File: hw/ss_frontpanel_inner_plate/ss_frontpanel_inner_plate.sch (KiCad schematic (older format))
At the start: 32 parts, among them J1 FFC_conn_14p, J2 FFC_conn_14p, J3 FFC_conn_14p, M1 Mousebite_stamp_holes, M2 Mousebite_stamp_holes, M3 Mousebite_stamp_holes, M4 FFC_retention_clamp, M5 FFC_retention_clamp, U6 TLV9051SIDBV

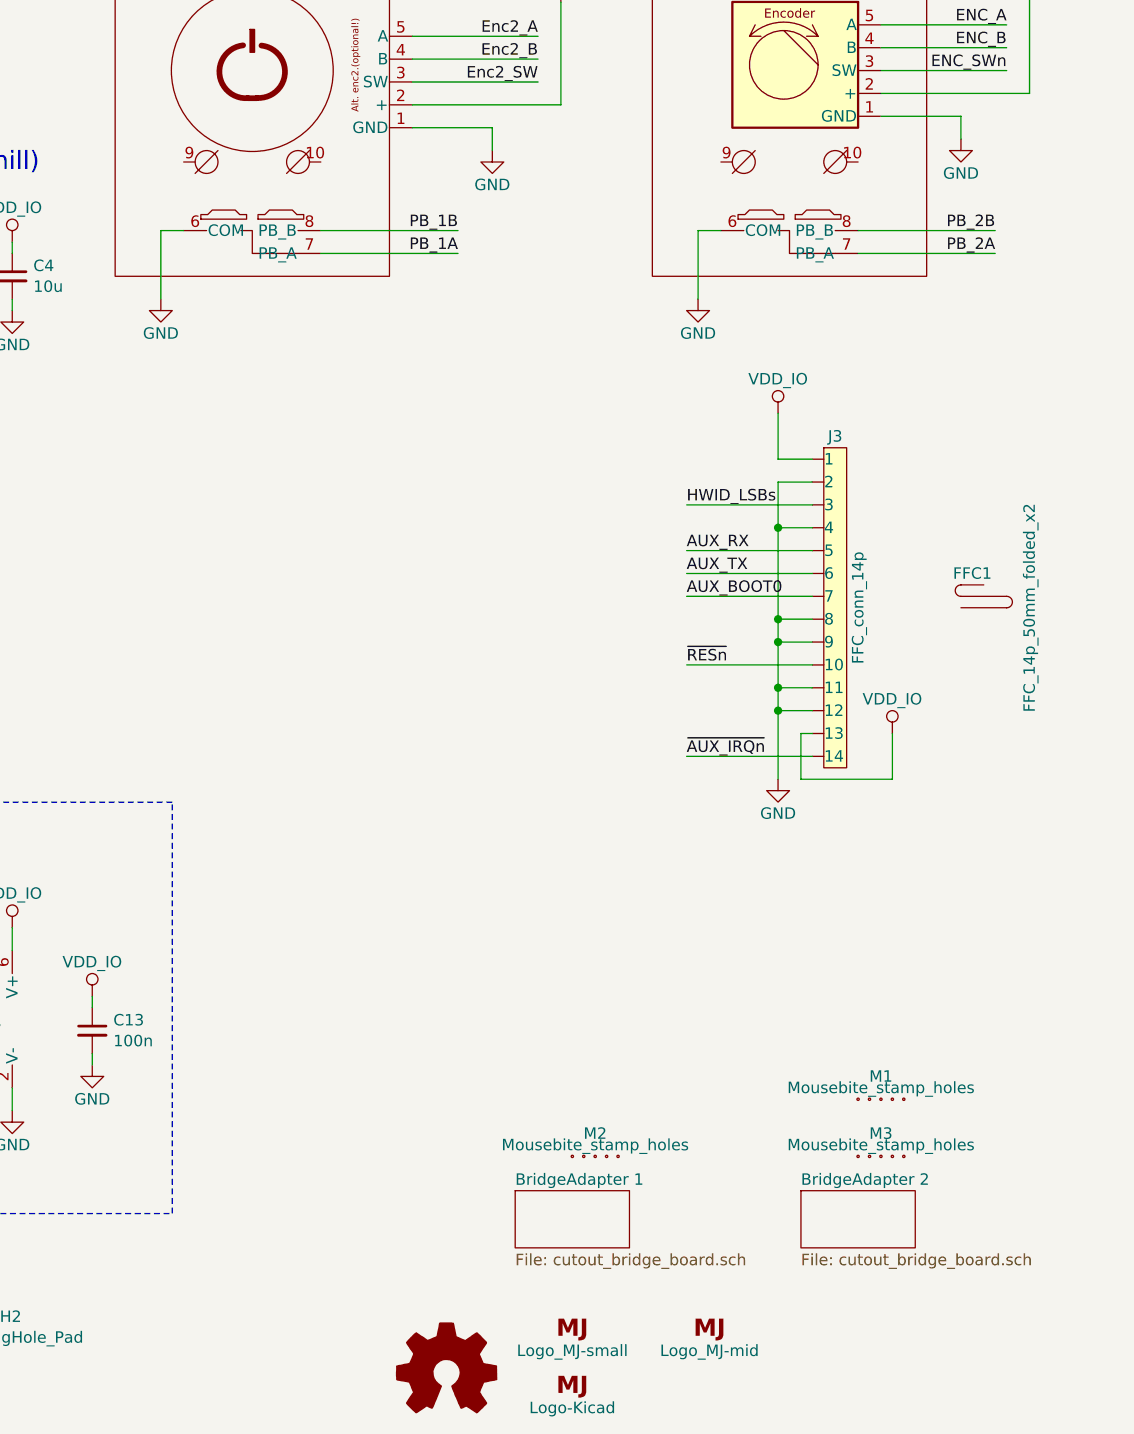
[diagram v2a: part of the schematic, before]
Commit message: Update frontpanel-inner-plate: Remove breakaway subboards; slight improve routing and plane fills. R2A files generated but not ordered
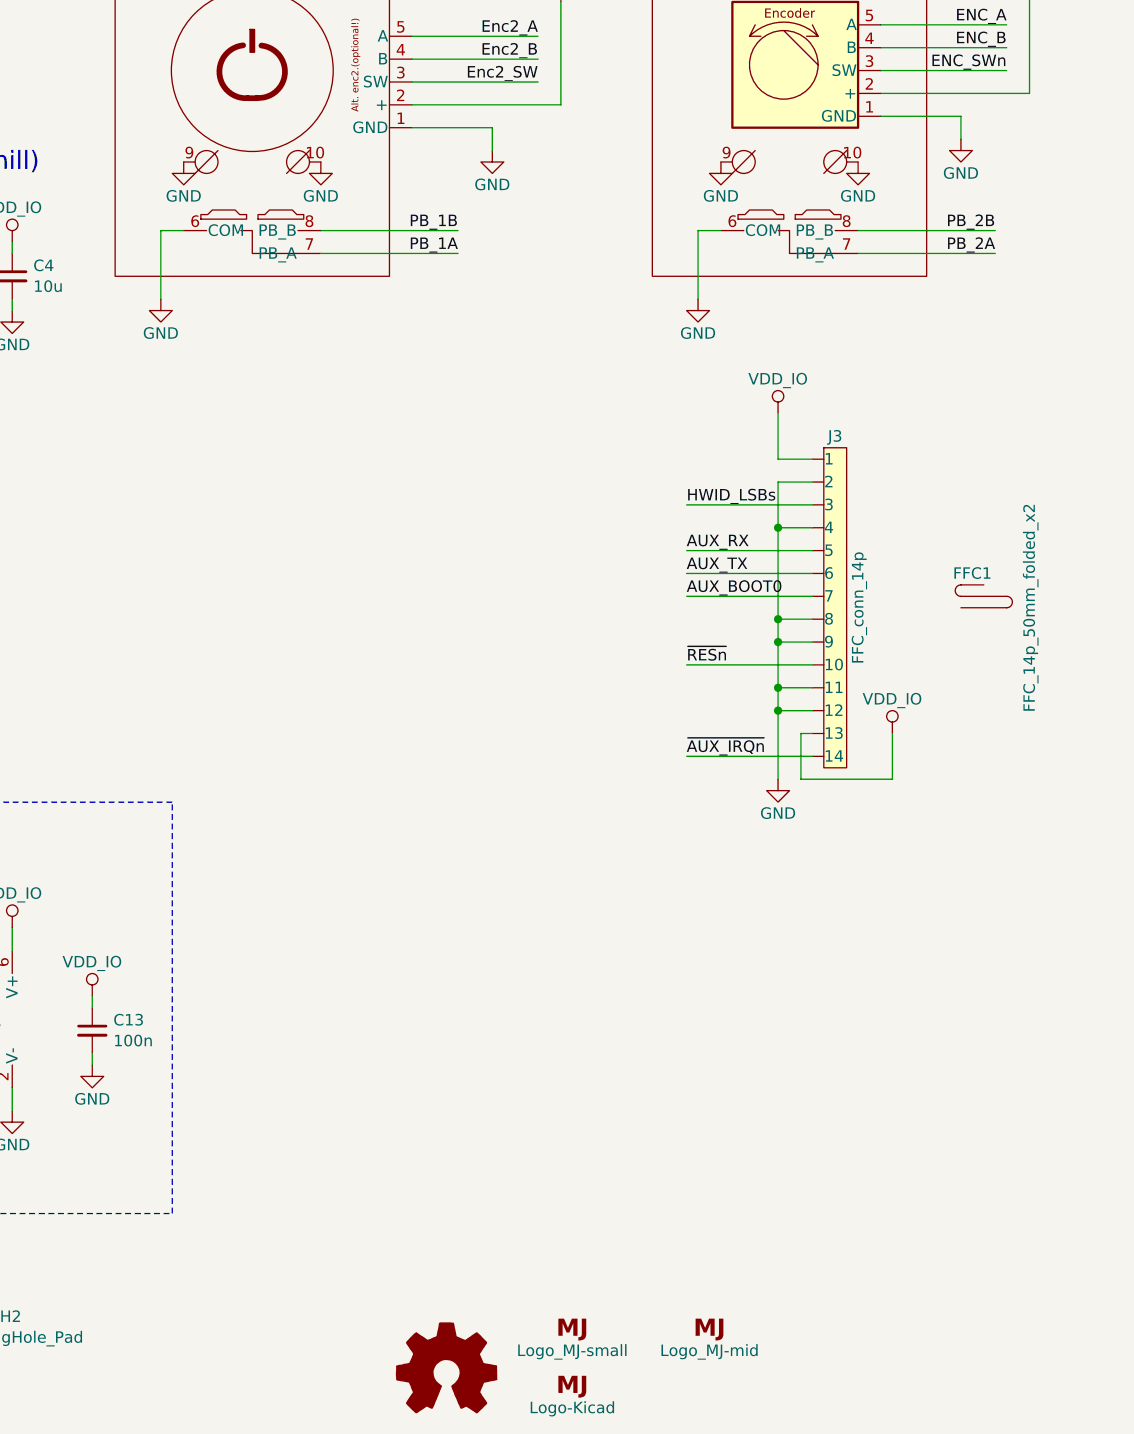
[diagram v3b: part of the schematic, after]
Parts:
- removed M1, M2, M3: Mousebite_stamp_holes, customlib_mj_fp:mousebite_5mm_stampholes, symbol customlib_mj:Mousebite_stamp_holes
- OLED1: footprint customlib_mj_fp:NHD3_12-Flush_with_bridge_cutouts -> customlib_mj_fp:NHD3_12-Flush_without_bridge_cutouts
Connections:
- net GND: now also ASM1.10, ASM1.9, ASM2.10, ASM2.9
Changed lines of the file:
@@
 F 0 "OLED1" H 2950 3550 50  0000 C CNN
 F 1 "NHD-3.12-25664" H 2950 3450 50  0000 C CNN
-F 2 "customlib_mj_fp:NHD3_12-Flush_with_bridge_cutouts" H 2950 3200 50  0001 C CNN
+F 2 "customlib_mj_fp:NHD3_12-Flush_without_bridge_cutouts" H 2950 3200 50  0001 C CNN
 F 3 "https://www.newhavendisplay.com/specs/NHD-3.12-25664UCW2.pdf" H 2950 3200 50  0001 C CNN
 	1    2950 3200
@@
 Wire Notes Line
 	7250 4400 4650 4400
-$Sheet
-S 8750 6100 500  250
-U 5F94C41C
-F0 "BridgeAdapter 1" 50
-F1 "cutout_bridge_board.sch" 50
-$EndSheet
-$Sheet
-S 10000 6100 500  250
-U 5F94C9C0
-F0 "BridgeAdapter 2" 50
-F1 "cutout_bridge_board.sch" 50
-$EndSheet
 Wire Wire Line
 	10050 3200 9900 3200
@@
 Wire Wire Line
 	9900 3200 9900 3000
-$Comp
-L customlib_mj:Mousebite_stamp_holes M2
-U 1 1 5FAD9C7F
-P 9100 5950
-F 0 "M2" H 9100 5850 50  0000 C CNN
-F 1 "Mousebite_stamp_holes" H 9100 5900 50  0000 C CNN
-F 2 "customlib_mj_fp:mousebite_5mm_stampholes" H 9100 5950 50  0001 C CNN
-F 3 "" H 9100 5950 50  0001 C CNN
-	1    9100 5950
-	-1   0    0    1
-$EndComp
-$Comp
-L customlib_mj:Mousebite_stamp_holes M1
-U 1 1 5FADA5BC
-P 10350 5700
-F 0 "M1" H 10350 5600 50  0000 C CNN
-F 1 "Mousebite_stamp_holes" H 10350 5650 50  0000 C CNN
-F 2 "customlib_mj_fp:mousebite_5mm_stampholes" H 10350 5700 50  0001 C CNN
-F 3 "" H 10350 5700 50  0001 C CNN
-	1    10350 5700
-	-1   0    0    1
-$EndComp
-$Comp
-L customlib_mj:Mousebite_stamp_holes M3
-U 1 1 5FADAC8E
-P 10350 5950
-F 0 "M3" H 10350 5850 50  0000 C CNN
-F 1 "Mousebite_stamp_holes" H 10350 5900 50  0000 C CNN
-F 2 "customlib_mj_fp:mousebite_5mm_stampholes" H 10350 5950 50  0001 C CNN
-F 3 "" H 10350 5950 50  0001 C CNN
-	1    10350 5950
-	-1   0    0    1
-$EndComp
 $Comp
 L customlib_mj:FFC_14p_50mm_folded_x2 FFC1
@@
 	1    0    0    -1
 $EndComp
+$Comp
+L power:GND #PWR0107
+U 1 1 60CF69EE
+P 7300 1600
+F 0 "#PWR0107" H 7300 1350 50  0001 C CNN
+F 1 "GND" H 7300 1450 50  0000 C CNN
+F 2 "" H 7300 1600 50  0001 C CNN
+F 3 "" H 7300 1600 50  0001 C CNN
+	1    7300 1600
+	1    0    0    -1
+$EndComp
+$Comp
+L power:GND #PWR0108
+U 1 1 60CF6CD0
+P 7900 1600
+F 0 "#PWR0108" H 7900 1350 50  0001 C CNN
+F 1 "GND" H 7900 1450 50  0000 C CNN
+F 2 "" H 7900 1600 50  0001 C CNN
+F 3 "" H 7900 1600 50  0001 C CNN
+	1    7900 1600
+	1    0    0    -1
+$EndComp
+$Comp
+L power:GND #PWR0109
+U 1 1 60CF7164
+P 9650 1600
+F 0 "#PWR0109" H 9650 1350 50  0001 C CNN
+F 1 "GND" H 9650 1450 50  0000 C CNN
+F 2 "" H 9650 1600 50  0001 C CNN
+F 3 "" H 9650 1600 50  0001 C CNN
+	1    9650 1600
+	1    0    0    -1
+$EndComp
+$Comp
+L power:GND #PWR0110
+U 1 1 60CF7511
+P 10250 1600
+F 0 "#PWR0110" H 10250 1350 50  0001 C CNN
+F 1 "GND" H 10250 1450 50  0000 C CNN
+F 2 "" H 10250 1600 50  0001 C CNN
+F 3 "" H 10250 1600 50  0001 C CNN
+	1    10250 1600
+	1    0    0    -1
+$EndComp
